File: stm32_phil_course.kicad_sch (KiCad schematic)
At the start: 16 parts

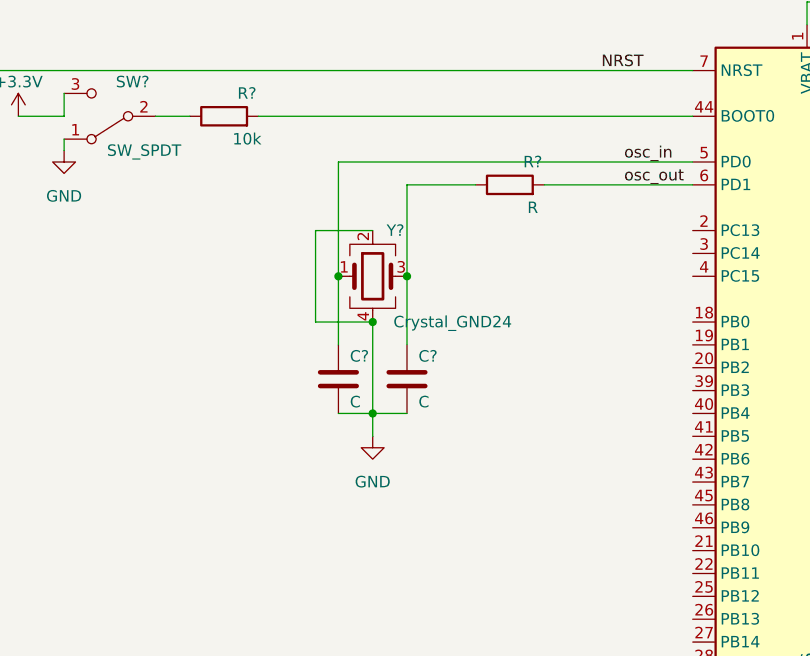
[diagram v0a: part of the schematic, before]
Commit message: add 4 pins crystal oscillator to schematic.
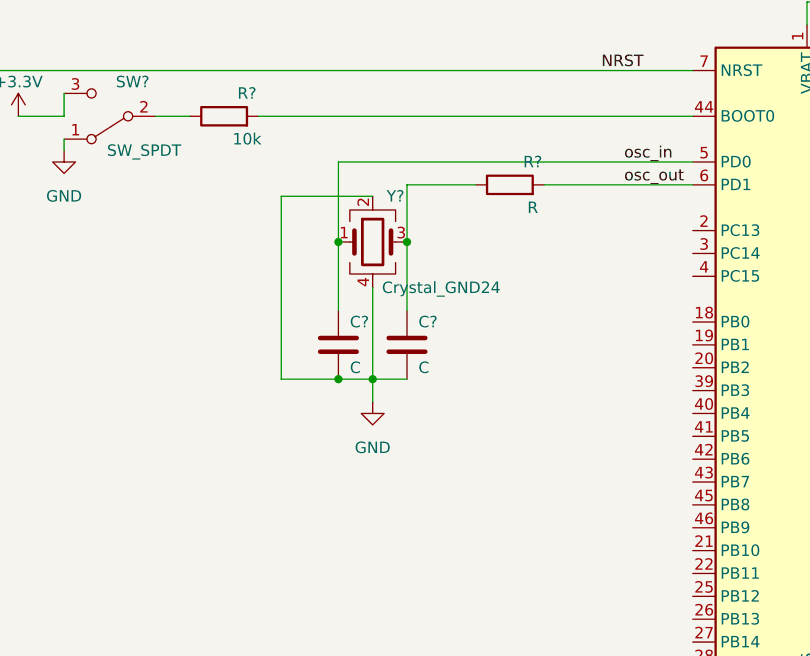
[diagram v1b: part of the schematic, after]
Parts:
- removed Y?: Crystal_GND24, symbol Device:Crystal_GND24
- added Y?: Crystal_GND24, symbol Device:Crystal_GND24
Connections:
- net GND: now also Y?.2, Y?.4
- net osc_in: now also Y?.1
- net at C?.1, R?.1: now also Y?.3
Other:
- moved on the sheet: C?
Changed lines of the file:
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@@
   (junction (at 144.78 53.34) (diameter 0) (color 0 0 0 0)
   )
-  (junction (at 97.79 83.82) (diameter 0) (color 0 0 0 0)
-  )
   (junction (at 97.79 34.29) (diameter 0) (color 0 0 0 0)
   )
+  (junction (at 90.17 95.25) (diameter 0) (color 0 0 0 0)
+  )
   (junction (at 194.31 34.29) (diameter 0) (color 0 0 0 0)
   )
-  (junction (at 90.17 83.82) (diameter 0) (color 0 0 0 0)
+  (junction (at 97.79 80.01) (diameter 0) (color 0 0 0 0)
   )
   (junction (at 110.49 34.29) (diameter 0) (color 0 0 0 0)
@@
   (junction (at 161.29 34.29) (diameter 0) (color 0 0 0 0)
   )
+  (junction (at 90.17 80.01) (diameter 0) (color 0 0 0 0)
+  )
   (junction (at 144.78 134.62) (diameter 0) (color 0 0 0 0)
   )
@@
   (junction (at 147.32 134.62) (diameter 0) (color 0 0 0 0)
   )
-  (junction (at 93.98 88.9) (diameter 0) (color 0 0 0 0)
-  )
-  (junction (at 93.98 99.06) (diameter 0) (color 0 0 0 0)
+  (junction (at 93.98 95.25) (diameter 0) (color 0 0 0 0)
   )
   (junction (at 146.05 53.34) (diameter 0) (color 0 0 0 0)
@@
     (stroke (width 0) (type default) (color 0 0 0 0))
   )
-  (wire (pts (xy 97.79 73.66) (xy 97.79 83.82))
+  (wire (pts (xy 83.82 74.93) (xy 83.82 95.25))
     (stroke (width 0) (type default) (color 0 0 0 0))
   )
@@
     (stroke (width 0) (type default) (color 0 0 0 0))
   )
-  (wire (pts (xy 90.17 83.82) (xy 90.17 91.44))
-    (stroke (width 0) (type default) (color 0 0 0 0))
-  )
-  (wire (pts (xy 93.98 88.9) (xy 93.98 99.06))
-    (stroke (width 0) (type default) (color 0 0 0 0))
-  )
-  (wire (pts (xy 87.63 78.74) (xy 87.63 88.9))
+  (wire (pts (xy 93.98 74.93) (xy 83.82 74.93))
     (stroke (width 0) (type default) (color 0 0 0 0))
   )
@@
     (stroke (width 0) (type default) (color 0 0 0 0))
   )
-  (wire (pts (xy 97.79 99.06) (xy 93.98 99.06))
+  (wire (pts (xy 97.79 95.25) (xy 93.98 95.25))
+    (stroke (width 0) (type default) (color 0 0 0 0))
+  )
+  (wire (pts (xy 97.79 73.66) (xy 97.79 80.01))
     (stroke (width 0) (type default) (color 0 0 0 0))
   )
@@
     (stroke (width 0) (type default) (color 0 0 0 0))
   )
+  (wire (pts (xy 93.98 85.09) (xy 93.98 95.25))
+    (stroke (width 0) (type default) (color 0 0 0 0))
+  )
   (wire (pts (xy 146.05 134.62) (xy 147.32 134.62))
     (stroke (width 0) (type default) (color 0 0 0 0))
@@
     (stroke (width 0) (type default) (color 0 0 0 0))
   )
+  (wire (pts (xy 90.17 80.01) (xy 90.17 87.63))
+    (stroke (width 0) (type default) (color 0 0 0 0))
+  )
   (wire (pts (xy 149.86 53.34) (xy 149.86 55.88))
     (stroke (width 0) (type default) (color 0 0 0 0))
@@
     (stroke (width 0) (type default) (color 0 0 0 0))
   )
-  (wire (pts (xy 90.17 71.12) (xy 90.17 83.82))
-    (stroke (width 0) (type default) (color 0 0 0 0))
-  )
-  (wire (pts (xy 93.98 99.06) (xy 93.98 101.6))
+  (wire (pts (xy 90.17 71.12) (xy 90.17 80.01))
+    (stroke (width 0) (type default) (color 0 0 0 0))
+  )
+  (wire (pts (xy 93.98 95.25) (xy 93.98 97.79))
     (stroke (width 0) (type default) (color 0 0 0 0))
   )
@@
     (stroke (width 0) (type default) (color 0 0 0 0))
   )
-  (wire (pts (xy 93.98 78.74) (xy 87.63 78.74))
-    (stroke (width 0) (type default) (color 0 0 0 0))
-  )
   (wire (pts (xy 85.09 41.91) (xy 97.79 41.91))
     (stroke (width 0) (type default) (color 0 0 0 0))
   )
-  (wire (pts (xy 97.79 83.82) (xy 97.79 91.44))
-    (stroke (width 0) (type default) (color 0 0 0 0))
-  )
   (wire (pts (xy 194.31 33.02) (xy 194.31 34.29))
     (stroke (width 0) (type default) (color 0 0 0 0))
@@
     (stroke (width 0) (type default) (color 0 0 0 0))
   )
-  (wire (pts (xy 87.63 88.9) (xy 93.98 88.9))
-    (stroke (width 0) (type default) (color 0 0 0 0))
-  )
-  (wire (pts (xy 90.17 99.06) (xy 93.98 99.06))
+  (wire (pts (xy 83.82 95.25) (xy 90.17 95.25))
     (stroke (width 0) (type default) (color 0 0 0 0))
   )
@@
     (stroke (width 0) (type default) (color 0 0 0 0))
   )
+  (wire (pts (xy 97.79 80.01) (xy 97.79 87.63))
+    (stroke (width 0) (type default) (color 0 0 0 0))
+  )
   (wire (pts (xy 146.05 53.34) (xy 144.78 53.34))
     (stroke (width 0) (type default) (color 0 0 0 0))
@@
   )
   (wire (pts (xy 104.14 41.91) (xy 104.14 45.72))
+    (stroke (width 0) (type default) (color 0 0 0 0))
+  )
+  (wire (pts (xy 90.17 95.25) (xy 93.98 95.25))
     (stroke (width 0) (type default) (color 0 0 0 0))
   )
@@
     (pin "1")
   )
-  (symbol (lib_id "power:GND") (at 93.98 101.6 0) (unit 1)
-    (in_bom yes) (on_board yes) (fields_autoplaced)
-    (property "Reference" "#PWR?" (id 0) (at 93.98 107.95 0)
-      (effects (font (size 1.27 1.27)) hide)
-    )
-    (property "Value" "GND" (id 1) (at 93.98 106.68 0))
-    (property "Footprint" "" (id 2) (at 93.98 101.6 0)
-      (effects (font (size 1.27 1.27)) hide)
-    )
-    (property "Datasheet" "" (id 3) (at 93.98 101.6 0)
+  (symbol (lib_id "power:GND") (at 93.98 97.79 0) (unit 1)
+    (in_bom yes) (on_board yes) (fields_autoplaced)
+    (property "Reference" "#PWR?" (id 0) (at 93.98 104.14 0)
+      (effects (font (size 1.27 1.27)) hide)
+    )
+    (property "Value" "GND" (id 1) (at 93.98 102.87 0))
+    (property "Footprint" "" (id 2) (at 93.98 97.79 0)
+      (effects (font (size 1.27 1.27)) hide)
+    )
+    (property "Datasheet" "" (id 3) (at 93.98 97.79 0)
       (effects (font (size 1.27 1.27)) hide)
     )
@@
     (pin "1")
   )
+  (symbol (lib_id "Device:Crystal_GND24") (at 93.98 80.01 0) (unit 1)
+    (in_bom yes) (on_board yes)
+    (property "Reference" "Y?" (id 0) (at 96.52 74.93 0))
+    (property "Value" "Crystal_GND24" (id 1) (at 101.6 85.09 0))
+    (property "Footprint" "" (id 2) (at 93.98 80.01 0)
+      (effects (font (size 1.27 1.27)) hide)
+    )
+    (property "Datasheet" "~" (id 3) (at 93.98 80.01 0)
+      (effects (font (size 1.27 1.27)) hide)
+    )
+    (pin "1")
+    (pin "2")
+    (pin "3")
+    (pin "4")
+  )
   (symbol (lib_id "Device:C") (at 110.49 38.1 0) (unit 1)
     (in_bom yes) (on_board yes) (fields_autoplaced)
@@
     (pin "2")
   )
-  (symbol (lib_id "Device:C") (at 90.17 95.25 0) (unit 1)
+  (symbol (lib_id "Device:C") (at 90.17 91.44 0) (unit 1)
     (in_bom yes) (on_board yes)
-    (property "Reference" "C?" (id 0) (at 91.44 92.71 0)
-      (effects (font (size 1.27 1.27)) (justify left))
-    )
-    (property "Value" "C" (id 1) (at 91.44 97.79 0)
-      (effects (font (size 1.27 1.27)) (justify left))
-    )
-    (property "Footprint" "" (id 2) (at 91.1352 99.06 0)
-      (effects (font (size 1.27 1.27)) hide)
-    )
-    (property "Datasheet" "~" (id 3) (at 90.17 95.25 0)
+    (property "Reference" "C?" (id 0) (at 91.44 88.9 0)
+      (effects (font (size 1.27 1.27)) (justify left))
+    )
+    (property "Value" "C" (id 1) (at 91.44 93.98 0)
+      (effects (font (size 1.27 1.27)) (justify left))
+    )
+    (property "Footprint" "" (id 2) (at 91.1352 95.25 0)
+      (effects (font (size 1.27 1.27)) hide)
+    )
+    (property "Datasheet" "~" (id 3) (at 90.17 91.44 0)
       (effects (font (size 1.27 1.27)) hide)
     )
@@
     (pin "1")
   )
-  (symbol (lib_id "Device:C") (at 97.79 95.25 0) (unit 1)
+  (symbol (lib_id "Device:C") (at 97.79 91.44 0) (unit 1)
     (in_bom yes) (on_board yes)
-    (property "Reference" "C?" (id 0) (at 99.06 92.71 0)
-      (effects (font (size 1.27 1.27)) (justify left))
-    )
-    (property "Value" "C" (id 1) (at 99.06 97.79 0)
-      (effects (font (size 1.27 1.27)) (justify left))
-    )
-    (property "Footprint" "" (id 2) (at 98.7552 99.06 0)
-      (effects (font (size 1.27 1.27)) hide)
-    )
-    (property "Datasheet" "~" (id 3) (at 97.79 95.25 0)
-      (effects (font (size 1.27 1.27)) hide)
-    )
-    (pin "1")
-    (pin "2")
-  )
-  (symbol (lib_id "Device:Crystal_GND24") (at 93.98 83.82 0) (unit 1)
-    (in_bom yes) (on_board yes)
-    (property "Reference" "Y?" (id 0) (at 96.52 78.74 0))
-    (property "Value" "Crystal_GND24" (id 1) (at 102.87 88.9 0))
-    (property "Footprint" "" (id 2) (at 93.98 83.82 0)
-      (effects (font (size 1.27 1.27)) hide)
-    )
-    (property "Datasheet" "~" (id 3) (at 93.98 83.82 0)
-      (effects (font (size 1.27 1.27)) hide)
-    )
-    (pin "1")
-    (pin "2")
-    (pin "3")
-    (pin "4")
+    (property "Reference" "C?" (id 0) (at 99.06 88.9 0)
+      (effects (font (size 1.27 1.27)) (justify left))
+    )
+    (property "Value" "C" (id 1) (at 99.06 93.98 0)
+      (effects (font (size 1.27 1.27)) (justify left))
+    )
+    (property "Footprint" "" (id 2) (at 98.7552 95.25 0)
+      (effects (font (size 1.27 1.27)) hide)
+    )
+    (property "Datasheet" "~" (id 3) (at 97.79 91.44 0)
+      (effects (font (size 1.27 1.27)) hide)
+    )
+    (pin "1")
+    (pin "2")
   )
   (symbol (lib_id "Device:R") (at 77.47 66.04 90) (unit 1)
@@
       (reference "U?") (unit 1) (value "STM32F103C8T6") (footprint "Package_QFP:LQFP-48_7x7mm_P0.5mm")
     )
-    (path "/ac5b2370-b44d-46c3-8f04-430447004b96"
+    (path "/6a6670cf-0ee9-4d1f-acef-5a1df8d19cc1"
       (reference "Y?") (unit 1) (value "Crystal_GND24") (footprint "")
     )

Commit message: remove r_ext from oscillator circuitry.
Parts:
- removed R?: R, symbol Device:R
- C? (x2): value C -> 27pF
- Y?: value Crystal_GND24 -> 16MHz
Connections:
- net osc_out: now also C?.1, Y?.3
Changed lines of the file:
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@@
     (stroke (width 0) (type default) (color 0 0 0 0))
   )
-  (wire (pts (xy 105.41 73.66) (xy 97.79 73.66))
+  (wire (pts (xy 97.79 73.66) (xy 129.54 73.66))
     (stroke (width 0) (type default) (color 0 0 0 0))
   )
@@
   )
   (wire (pts (xy 104.14 41.91) (xy 110.49 41.91))
-    (stroke (width 0) (type default) (color 0 0 0 0))
-  )
-  (wire (pts (xy 113.03 73.66) (xy 129.54 73.66))
     (stroke (width 0) (type default) (color 0 0 0 0))
   )
@@
     (in_bom yes) (on_board yes)
     (property "Reference" "Y?" (id 0) (at 96.52 74.93 0))
-    (property "Value" "Crystal_GND24" (id 1) (at 101.6 85.09 0))
+    (property "Value" "16MHz" (id 1) (at 97.79 85.09 0))
     (property "Footprint" "" (id 2) (at 93.98 80.01 0)
       (effects (font (size 1.27 1.27)) hide)
@@
       (effects (font (size 1.27 1.27)) (justify left))
     )
-    (property "Value" "C" (id 1) (at 91.44 93.98 0)
+    (property "Value" "27pF" (id 1) (at 91.44 93.98 0)
       (effects (font (size 1.27 1.27)) (justify left))
     )
@@
       (effects (font (size 1.27 1.27)) (justify left))
     )
-    (property "Value" "C" (id 1) (at 99.06 93.98 0)
+    (property "Value" "27pF" (id 1) (at 99.06 93.98 0)
       (effects (font (size 1.27 1.27)) (justify left))
     )
@@
     (pin "1")
   )
-  (symbol (lib_id "Device:R") (at 109.22 73.66 90) (unit 1)
-    (in_bom yes) (on_board yes)
-    (property "Reference" "R?" (id 0) (at 111.76 71.12 90))
-    (property "Value" "R" (id 1) (at 111.76 76.2 90))
-    (property "Footprint" "" (id 2) (at 109.22 75.438 90)
-      (effects (font (size 1.27 1.27)) hide)
-    )
-    (property "Datasheet" "~" (id 3) (at 109.22 73.66 0)
-      (effects (font (size 1.27 1.27)) hide)
-    )
-    (pin "1")
-    (pin "2")
-  )
   (sheet_instances
     (path "/" (page "1"))
@@
     )
     (path "/92290c52-0f88-4f4d-9ee0-bc442b80a14a"
-      (reference "C?") (unit 1) (value "C") (footprint "")
+      (reference "C?") (unit 1) (value "27pF") (footprint "")
     )
     (path "/aa63328e-47bb-42c8-bb7a-616e07fee189"
-      (reference "C?") (unit 1) (value "C") (footprint "")
+      (reference "C?") (unit 1) (value "27pF") (footprint "")
     )
     (path "/db7da312-326a-4d3d-8547-ca56497b7eee"
@@
       (reference "R?") (unit 1) (value "10k") (footprint "")
     )
-    (path "/e281250e-9e2c-41d1-b03e-003ec2106dc4"
-      (reference "R?") (unit 1) (value "R") (footprint "")
-    )
     (path "/25bdde6c-70d8-450d-b468-708a71dc607f"
       (reference "SW?") (unit 1) (value "SW_SPDT") (footprint "")
@@
     )
     (path "/6a6670cf-0ee9-4d1f-acef-5a1df8d19cc1"
-      (reference "Y?") (unit 1) (value "Crystal_GND24") (footprint "")
-    )
-  )
+      (reference "Y?") (unit 1) (value "16MHz") (footprint "")
+    )
+  )

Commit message: finish oscillator circuitry.
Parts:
- Y?: value 16MHz -> 16MHz_abm8
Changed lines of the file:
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@@
     (in_bom yes) (on_board yes)
     (property "Reference" "Y?" (id 0) (at 96.52 74.93 0))
-    (property "Value" "16MHz" (id 1) (at 97.79 85.09 0))
+    (property "Value" "16MHz_abm8" (id 1) (at 100.33 85.09 0))
     (property "Footprint" "" (id 2) (at 93.98 80.01 0)
       (effects (font (size 1.27 1.27)) hide)
@@
     )
     (path "/6a6670cf-0ee9-4d1f-acef-5a1df8d19cc1"
-      (reference "Y?") (unit 1) (value "16MHz") (footprint "")
-    )
-  )
+      (reference "Y?") (unit 1) (value "16MHz_abm8") (footprint "")
+    )
+  )
